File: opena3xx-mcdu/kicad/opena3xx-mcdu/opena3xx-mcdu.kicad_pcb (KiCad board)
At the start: 2 copper layers, 148 x 225 mm, 149 parts, among them J1 Conn_02x01, J2 Conn_02x01, J3 Conn_02x01, J4 Conn_02x01, J5 Conn_02x01, J6 Conn_02x01, J7 Conn_02x01, J8 Conn_02x01, SW1 TLL-6A, SW10 TLL-6A, SW100 SW_MEC_5E, SW11 TLL-6A, SW12 TLL-6A, SW13 TLL-6A, SW14 TLL-6A, SW15 TLL-6A, SW16 TLL-6A, SW17 TLL-6A, SW18 TLL-6A, SW19 TLL-6A, SW2 TLL-6A, SW20 TLL-6A, SW21 TLL-6A, SW22 TLL-6A, SW23 TLL-6A, SW24 TLL-6A, SW25 TLL-6A, SW26 TLL-6A, SW27 TLL-6A, SW28 TLL-6A, SW29 TLL-6A, SW3 TLL-6A, SW30 TLL-6A, SW31 TLL-6A, SW32 TLL-6A, SW33 TLL-6A, SW34 TLL-6A, SW35 TLL-6A, SW36 TLL-6A, SW37 TLL-6A, SW38 TLL-6A, SW39 TLL-6A, SW4 TLL-6A, SW40 TLL-6A, SW41 TLL-6A, SW42 TLL-6A, SW43 TLL-6A, SW44 TLL-6A, SW45 TLL-6A, SW46 TLL-6A, SW47 TLL-6A, SW48 TLL-6A, SW49 TLL-6A, SW5 TLL-6A, SW50 TLL-6A, SW51 TLL-6A, SW52 TLL-6A, SW53 TLL-6A, SW54 TLL-6A, SW55 TLL-6A, SW56 TLL-6A, SW57 TLL-6A, SW58 TLL-6A, SW59 TLL-6A, SW6 TLL-6A, SW60 TLL-6A, SW61 TLL-6A, SW62 TLL-6A, SW63 TLL-6A, SW64 TLL-6A, SW65 TLL-6A, SW66 TLL-6A, SW67 TLL-6A, SW68 TLL-6A, SW69 TLL-6A, SW7 TLL-6A, SW70 TLL-6A, SW71 TLL-6A, SW72 TLL-6A, SW73 TLL-6A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

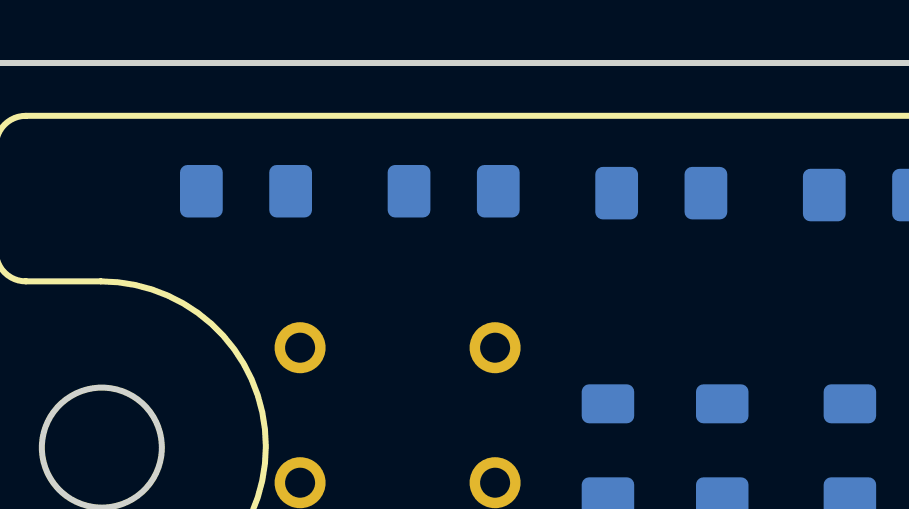
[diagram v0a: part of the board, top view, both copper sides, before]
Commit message: Fixed LED Markings + STP File Updated
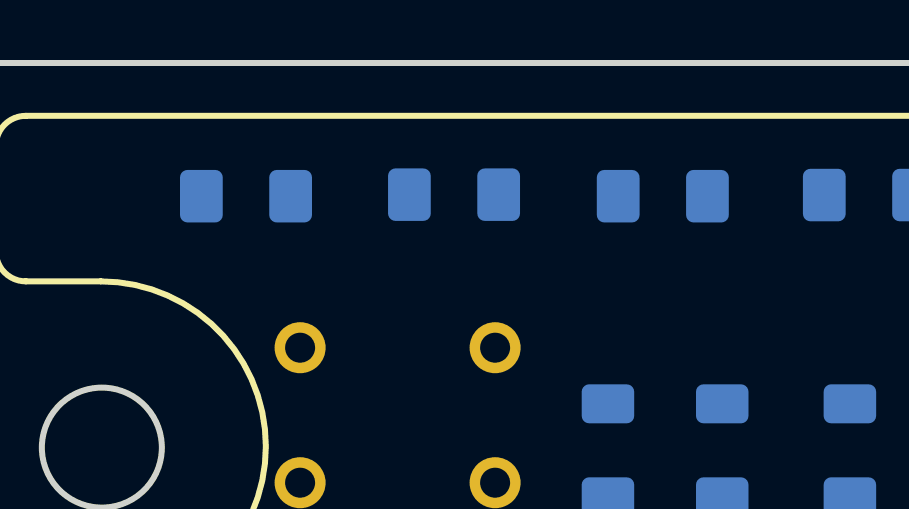
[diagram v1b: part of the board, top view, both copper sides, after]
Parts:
- added ?: , , F.Cu at (156.4, 34.0)
- added ?: , , F.Cu at (161.4, 34.5)
- added ?: , , F.Cu at (160.8, 34.3)
- D2: value YELLOW LED -> MESSAGING
- D4: value ORANGE LED -> SIGNAL
- moved D1 0.17 mm to (141.5, 32.1)
- moved D2 0.11 mm to (148.4, 32.0)
- moved D4 0.11 mm to (155.4, 32.1)
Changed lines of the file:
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@@
     (tracks 0)
     (zones 0)
-    (modules 149)
+    (modules 152)
     (nets 182)
   )
@@
     (add_net SIGNAL_LED)
   )
+  (module "" (layer F.Cu)
+    (at 156.3878 33.9852)
+    (fp_text reference "" (at 161.3662 34.544) (layer F.SilkS)
+      (effects (font (size 1.27 1.27) (thickness 0.15)))
+    )
+    (fp_text value "" (at 161.3662 34.544) (layer F.SilkS)
+      (effects (font (size 1.27 1.27) (thickness 0.15)))
+    )
+    (fp_text user FAULT (at 162.1912 34.0868 180) (layer B.SilkS)
+      (effects (font (size 1 1) (thickness 0.15)) (justify mirror))
+    )
+  )
+  (module "" (layer F.Cu)
+    (at 161.3662 34.544)
+    (fp_text reference "" (at 160.8074 34.29) (layer F.SilkS)
+      (effects (font (size 1.27 1.27) (thickness 0.15)))
+    )
+    (fp_text value "" (at 160.8074 34.29) (layer F.SilkS)
+      (effects (font (size 1.27 1.27) (thickness 0.15)))
+    )
+    (fp_text user FAULT (at 161.8864 33.8328 180) (layer B.SilkS)
+      (effects (font (size 1 1) (thickness 0.15)) (justify mirror))
+    )
+  )
+  (module "" (layer F.Cu)
+    (at 160.8074 34.29)
+    (fp_text reference "" (at 205.2574 57.7596) (layer F.SilkS)
+      (effects (font (size 1.27 1.27) (thickness 0.15)))
+    )
+    (fp_text value "" (at 205.2574 57.7596) (layer F.SilkS)
+      (effects (font (size 1.27 1.27) (thickness 0.15)))
+    )
+    (fp_text user FAULT (at 206.3364 57.8612 180) (layer B.SilkS)
+      (effects (font (size 1 1) (thickness 0.15)) (justify mirror))
+    )
+  )
   (module opena3x:Logo (layer B.Cu)
     (at 205.2574 57.7596 180)
@@
   )
   (module Diode_SMD:D_1206_3216Metric_Pad1.42x1.75mm_HandSolder (layer B.Cu)
-    (at 155.321 31.9532 180)
+    (at 155.3718 32.0548 180)
     (descr "Diode SMD 1206 (3216 Metric), square (rectangular) end terminal, IPC_7351 nominal, (Body size source: http://www.tortai-tech.com/upload/download/2011102023233369053.pdf), generated with kicad-footprint-generator")
     (tags "diode handsolder")
@@
       (effects (font (size 1 1) (thickness 0.15)) (justify mirror))
     )
-    (fp_text value "ORANGE LED" (at 0 -1.82) (layer B.Fab)
-      (effects (font (size 1 1) (thickness 0.15)) (justify mirror))
+    (fp_text value SIGNAL (at 0 -1.82) (layer B.SilkS)
+      (effects (font (size 1 0.8) (thickness 0.15)) (justify mirror))
     )
     (fp_line (start 2.45 -1.12) (end -2.45 -1.12) (layer B.CrtYd) (width 0.05))
@@
     )
     (fp_text value FAULT (at 0 -1.9685) (layer B.SilkS)
-      (effects (font (size 1 1) (thickness 0.15)) (justify mirror))
+      (effects (font (size 1 0.8) (thickness 0.15)) (justify mirror))
     )
     (fp_line (start 2.45 -1.12) (end -2.45 -1.12) (layer B.CrtYd) (width 0.05))
@@
   )
   (module Diode_SMD:D_1206_3216Metric_Pad1.42x1.75mm_HandSolder (layer B.Cu)
-    (at 148.4 31.8897 180)
+    (at 148.4122 32.004 180)
     (descr "Diode SMD 1206 (3216 Metric), square (rectangular) end terminal, IPC_7351 nominal, (Body size source: http://www.tortai-tech.com/upload/download/2011102023233369053.pdf), generated with kicad-footprint-generator")
     (tags "diode handsolder")
@@
       (effects (font (size 1 1) (thickness 0.15)) (justify mirror))
     )
-    (fp_text value "YELLOW LED" (at 0 -1.82) (layer B.Fab)
-      (effects (font (size 1 1) (thickness 0.15)) (justify mirror))
+    (fp_text value MESSAGING (at 0 -1.82) (layer B.SilkS)
+      (effects (font (size 1 0.8) (thickness 0.15)) (justify mirror))
     )
     (fp_line (start 2.45 -1.12) (end -2.45 -1.12) (layer B.CrtYd) (width 0.05))
@@
   )
   (module Diode_SMD:D_1206_3216Metric_Pad1.42x1.75mm_HandSolder (layer B.Cu)
-    (at 141.478 31.8897 180)
+    (at 141.478 32.0548 180)
     (descr "Diode SMD 1206 (3216 Metric), square (rectangular) end terminal, IPC_7351 nominal, (Body size source: http://www.tortai-tech.com/upload/download/2011102023233369053.pdf), generated with kicad-footprint-generator")
     (tags "diode handsolder")
@@
     )
     (fp_text value POWER (at 0 -1.82) (layer B.SilkS)
-      (effects (font (size 1 1) (thickness 0.14)) (justify mirror))
+      (effects (font (size 1 0.8) (thickness 0.14)) (justify mirror))
     )
     (fp_line (start 2.45 -1.12) (end -2.45 -1.12) (layer B.CrtYd) (width 0.05))
@@
   )
   (gr_text RESET (at 146.5834 43.7388) (layer B.SilkS)
-    (effects (font (size 1.5 1.5) (thickness 0.3)) (justify mirror))
+    (effects (font (size 1.5 1.5) (thickness 0.2)) (justify mirror))
   )
   (gr_text "+-       +-" (at 146.5834 225.298 270) (layer B.SilkS)

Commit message: Adding MCDU STL (PCB)
Adding MCDU STL (PCB)
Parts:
- moved C1 36.7 mm to (198.1, 110.9)
- moved C5 36.7 mm to (285.7, 110.9)
- moved D10 36.7 mm to (308.0, 194.4)
- moved D3 36.7 mm to (198.7, 27.4)
- moved D5 36.7 mm to (211.9, 29.5)
- moved G*** 36.7 mm to (241.7, 53.2)
- moved J5 36.7 mm to (217.5, 70.3)
- moved J6 36.7 mm to (310.4, 131.8)
- moved J7 36.7 mm to (310.4, 121.0)
- moved J8 36.7 mm to (310.3, 149.5)
- moved R24 36.7 mm to (225.5, 237.7)
- moved R25 36.7 mm to (271.5, 166.8)
- moved R26 36.7 mm to (241.5, 180.9)
- moved R29 36.7 mm to (301.9, 194.7)
- moved R30 36.7 mm to (271.5, 208.9)
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
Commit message: Adding @Kavster89 LCD Driver Board holes.
Adding @Kavster89 LCD Driver Board holes.
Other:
- outline, holes or cut-outs redrawn

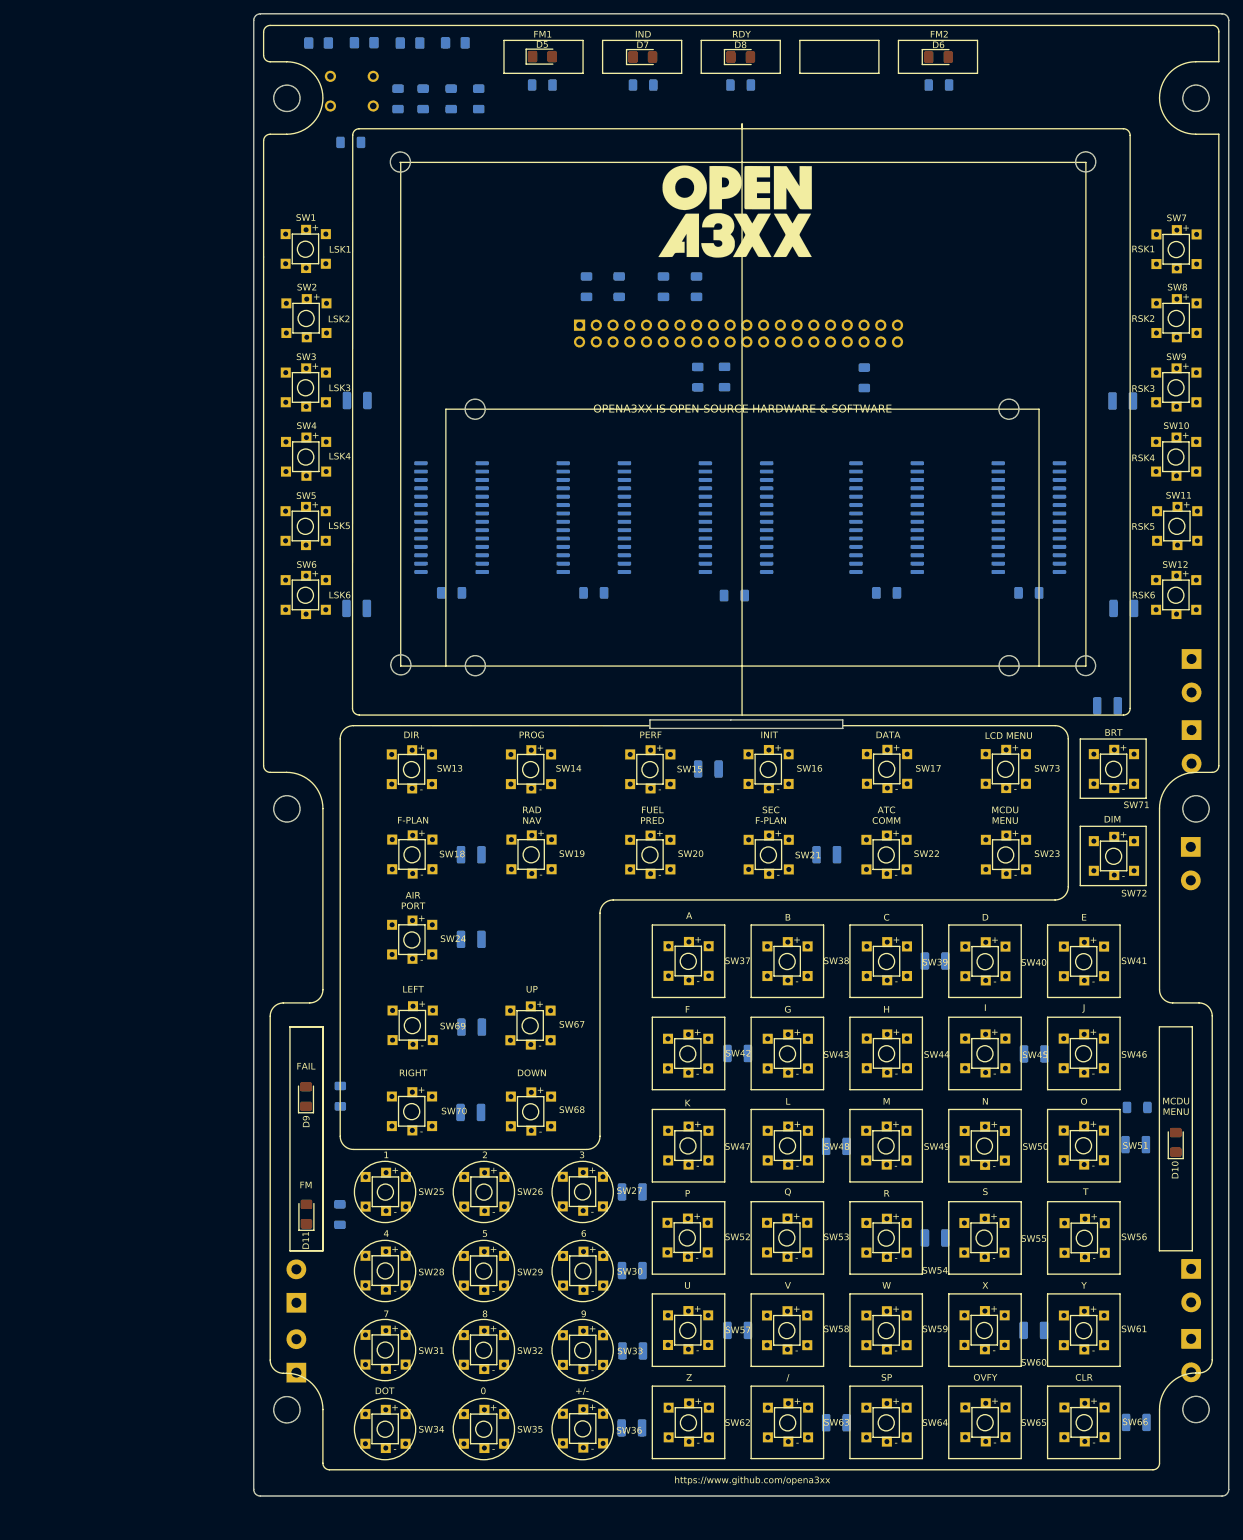
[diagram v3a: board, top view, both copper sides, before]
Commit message: MCDU Improvements Markings + Added Tactile for LCD Power + LED funcational names
MCDU Improvements Markings + Added Tactile for LCD Power + LED funcational names
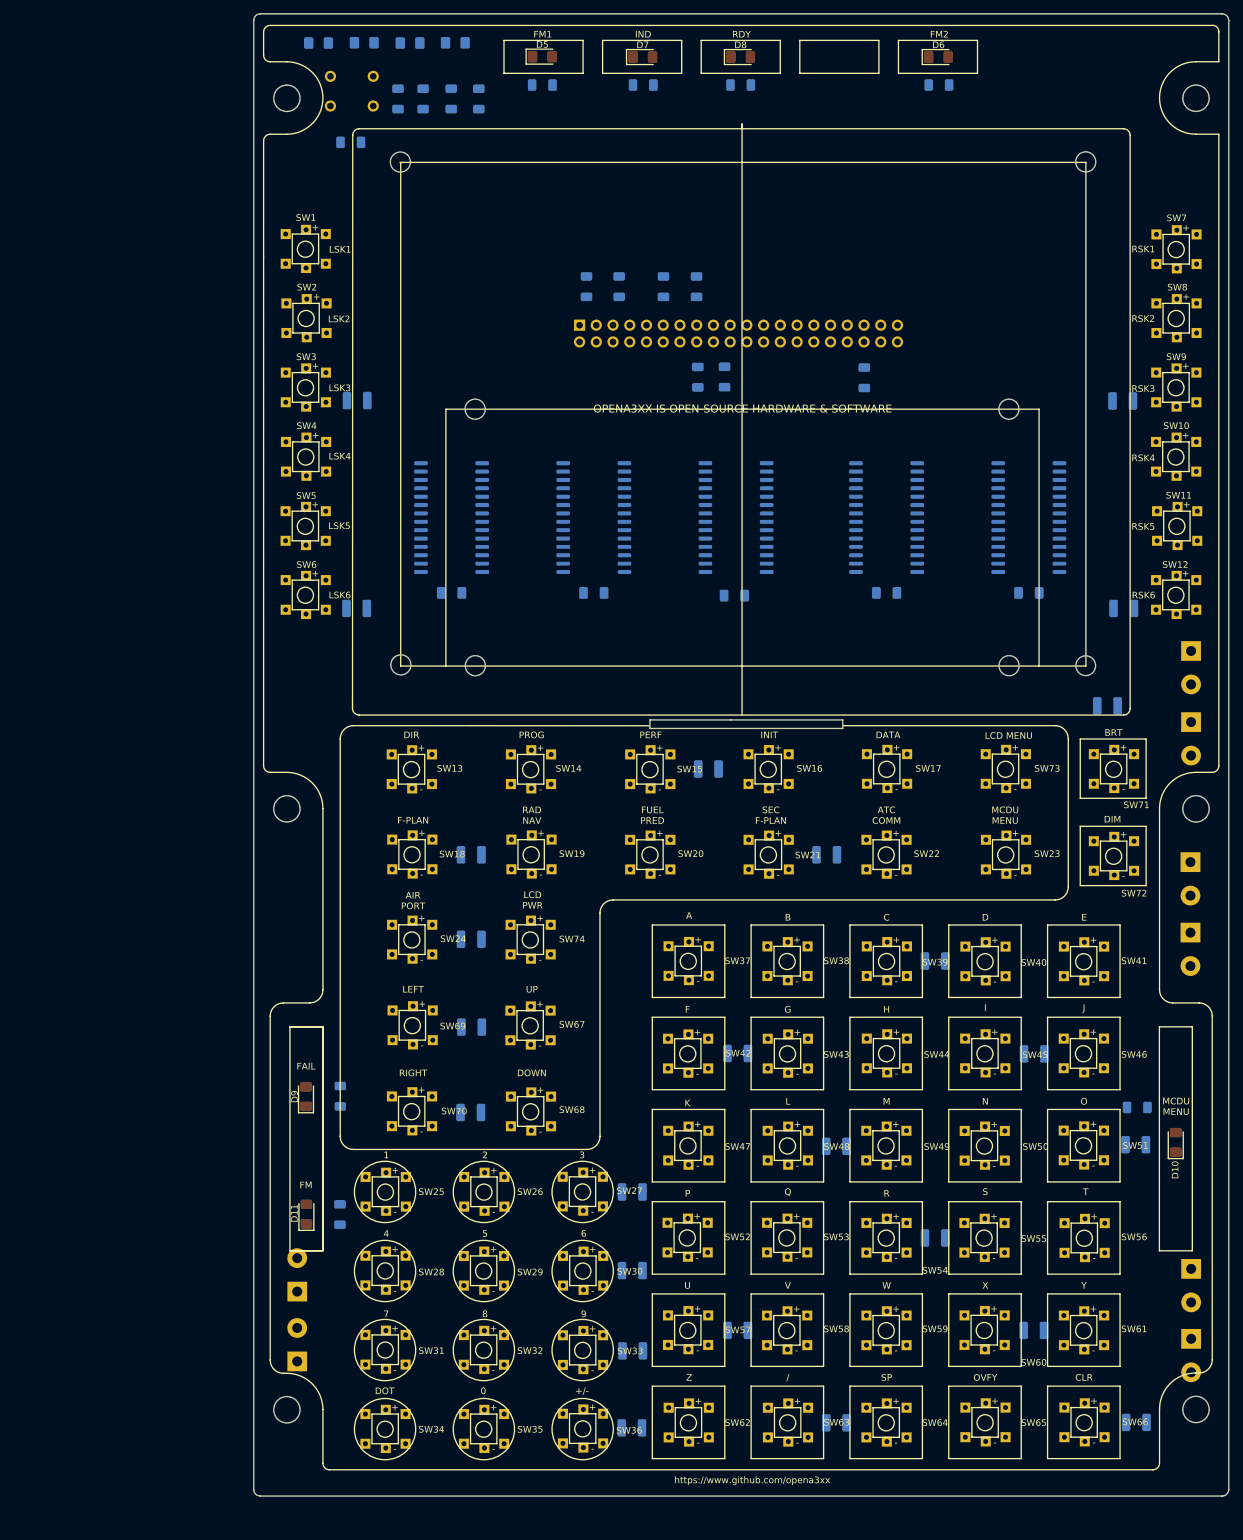
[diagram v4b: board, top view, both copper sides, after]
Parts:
- removed ? (x3): , 
- removed G*** (x2): LOGO, opena3x:Logo
- added J9: Conn_02x01, TerminalBlock:TerminalBlock_bornier-2_P5.08mm, B.Cu at (310.3, 162.5)
- added SW74: TLL-6A, opena3x:TACTILE_LED_TH, F.Cu at (211.0, 157.3)
- D2: value MESSAGING -> STATUS
- moved J8 2.31 mm to (310.3, 151.8)
- moved J1 1.71 mm to (174.7, 227.6)
- moved J2 1.71 mm to (174.7, 217.0)
- moved J6 1.22 mm to (310.3, 130.6)
- moved J7 1.22 mm to (310.3, 119.8)
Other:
- board text added: "LCD PWR"
